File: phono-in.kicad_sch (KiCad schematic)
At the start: 69 parts, among them J1 Conn_01x03_Pin, Q1 2N3906, Q10 2N3906, Q11 JFE2140D, Q12 2N5089, Q13 2N3904, Q14 2N3904, Q15 2N5089, Q16 2N5087, Q17 2N5087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

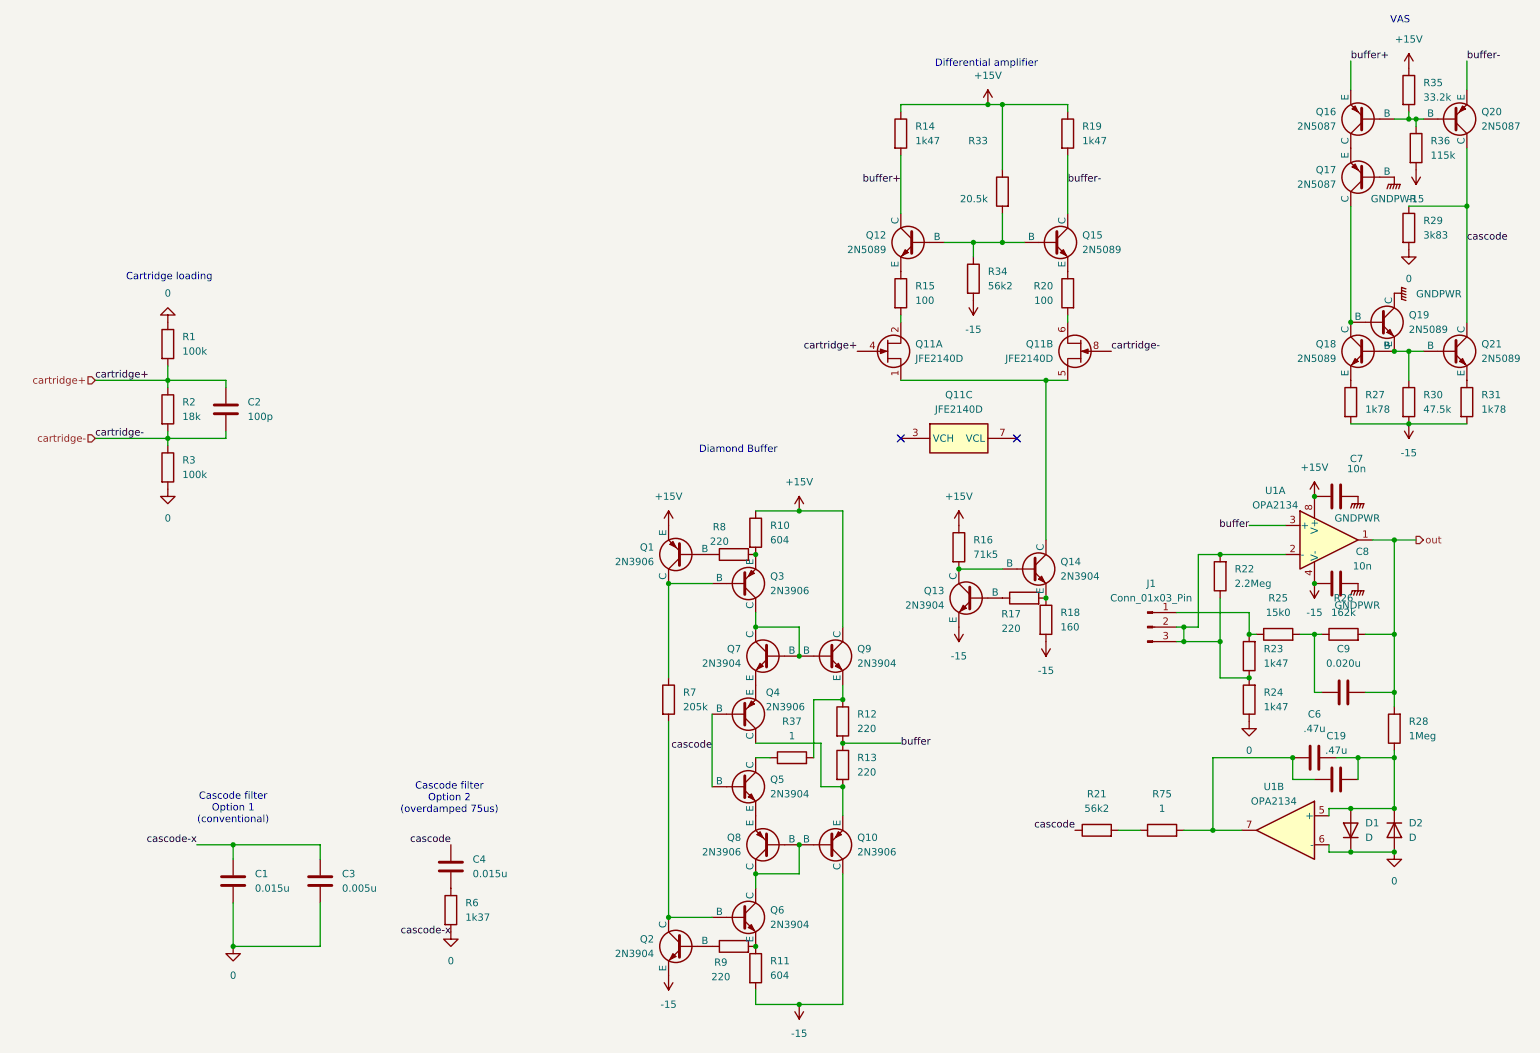
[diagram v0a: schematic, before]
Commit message: Revision 0.2
- TH components mounted to PCB back to preserve front space
- 15+ and 15- lines are kept closer together to reduce noise (even though di/dt is relatively low)
- Signal path bends around PCB area; DC servo feedback path is much shorter
- Signal path kept on first layer without jumpers

- Power distribution is messy
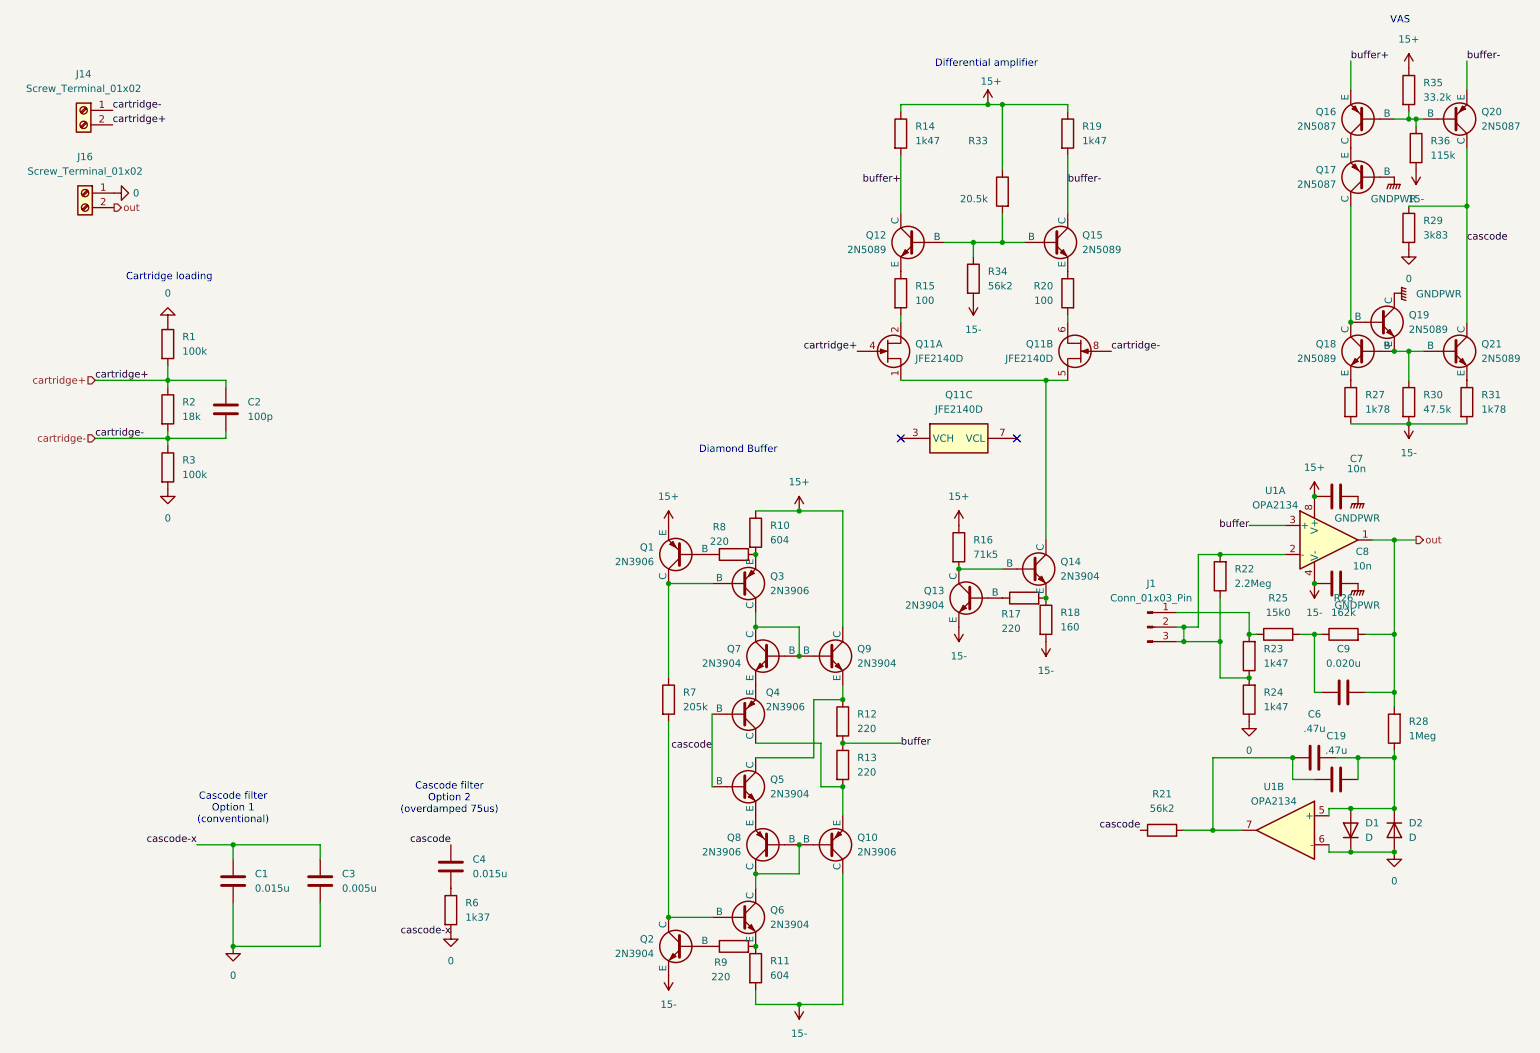
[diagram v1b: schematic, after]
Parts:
- removed R37, R75: 1, Resistor_SMD:R_0805_2012Metric_Pad1.20x1.40mm_HandSolder, symbol Device:R
- added J14, J16: Screw_Terminal_01x02, Library:TerminalBlock_4Ucon_1x02_P5mm_Horizontal, symbol Connector:Screw_Terminal_01x02
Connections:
- net 0: now also J16.1 (Pin_1)
- net cartridge+: now also J14.2 (Pin_2)
- net cartridge-: now also J14.1 (Pin_1)
- net out: now also J16.2 (Pin_2)
- net at R21.2: now also C19.2, C6.2, U1.7
- net at Q9.3 (E), R12.1: now also Q5.1 (C)
- net +15V renamed 15+
- net -15 renamed 15-
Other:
- moved on the sheet: R21

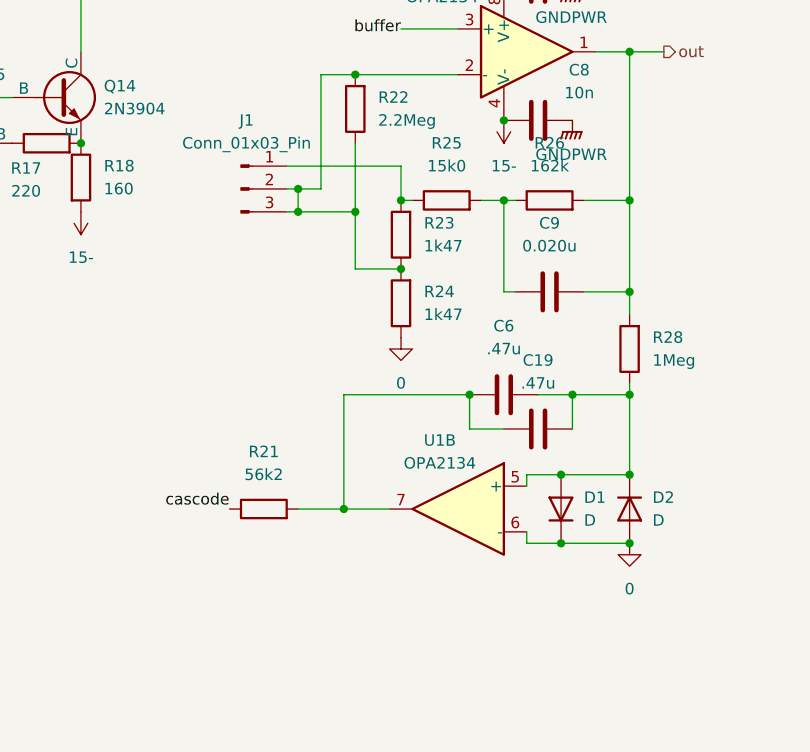
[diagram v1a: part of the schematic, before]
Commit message: Revision 0.3 - Fix reverse-wired DC servo - Reduce gain from 40 db to 35 db
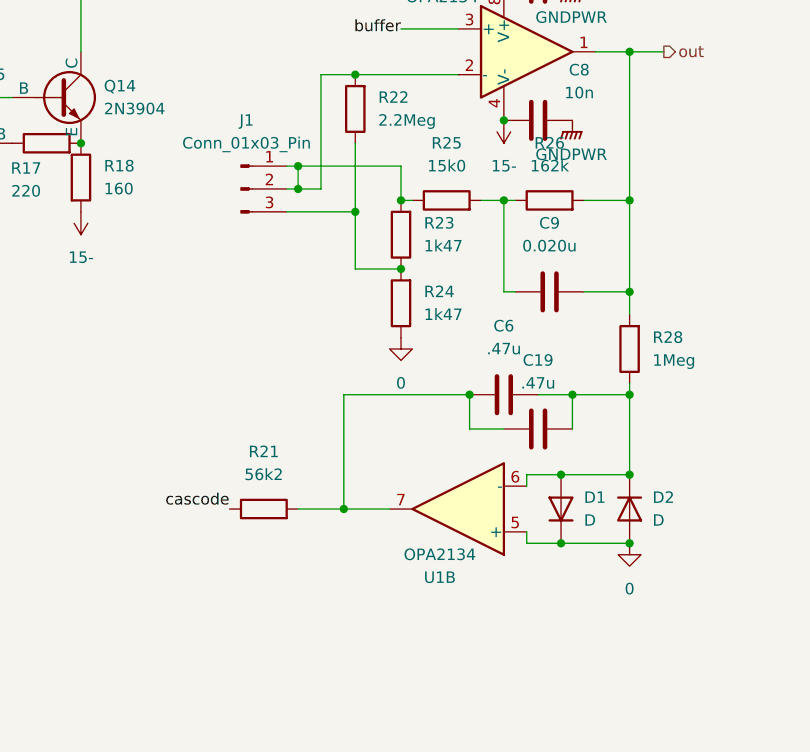
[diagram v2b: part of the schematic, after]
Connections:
- net 0: now also U1.5 (+); no longer U1.6 (-)
- net at J1.3 (Pin_3), R22.1, R23.1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: no longer J1.2 (Pin_2), R22.2, U1.2 (-)
- net at C19.1, C6.1, D1.2 (A)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: now also U1.6 (-); no longer U1.5 (+)
- net at J1.1 (Pin_1), R23.2, R25.1: now also J1.2 (Pin_2), R22.2, U1.2 (-)
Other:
- moved on the sheet: U1B
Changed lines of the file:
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@@
 	)
 	(junction
-		(at 223.52 123.19)
+		(at 223.52 120.65)
 		(diameter 0)
 		(color 0 0 0 0)
@@
 	)
 	(junction
-		(at 223.52 120.65)
-		(diameter 0)
-		(color 0 0 0 0)
-	)
-	(junction
 		(at 254 143.51)
 		(diameter 0)
@@
 	)
 	(junction
+		(at 223.52 118.11)
+		(diameter 0)
+		(color 0 0 0 0)
+	)
+	(junction
 		(at 252.73 152.4)
 		(diameter 0)
@@
 	(wire
 		(pts
-			(xy 223.52 120.65) (xy 223.52 123.19)
+			(xy 223.52 118.11) (xy 223.52 120.65)
 		)
 		(stroke
@@
 	(wire
 		(pts
+			(xy 223.52 118.11) (xy 234.95 118.11)
+		)
+		(stroke
+			(width 0)
+			(type default)
+		)
+	)
+	(wire
+		(pts
 			(xy 250.19 143.51) (xy 254 143.51)
 		)
@@
 	(wire
 		(pts
-			(xy 222.25 118.11) (xy 234.95 118.11)
+			(xy 222.25 118.11) (xy 223.52 118.11)
 		)
 		(stroke
@@
 	(wire
 		(pts
-			(xy 223.52 123.19) (xy 229.87 123.19)
-		)
-		(stroke
-			(width 0)
-			(type default)
-		)
-	)
-	(wire
-		(pts
 			(xy 254 143.51) (xy 260.35 143.51)
 		)
@@
 	(wire
 		(pts
-			(xy 222.25 123.19) (xy 223.52 123.19)
+			(xy 222.25 123.19) (xy 229.87 123.19)
 		)
 		(stroke
@@
 	(symbol
 		(lib_id "Amplifier_Operational:OPA2134")
-		(at 241.3 156.21 0)
-		(mirror y)
+		(at 241.3 156.21 180)
 		(unit 2)
 		(body_style 1)
@@
 		(dnp no)
 		(property "Reference" "U1"
-			(at 239.268 148.59 0)
+			(at 239.268 163.83 0)
 			(show_name no)
 			(do_not_autoplace no)
@@
 		)
 		(property "Value" "OPA2134"
-			(at 239.268 151.13 0)
+			(at 239.268 161.29 0)
 			(show_name no)
 			(do_not_autoplace no)
